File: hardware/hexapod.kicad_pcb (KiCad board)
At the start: 2 copper layers, 99.9 x 85.9 mm, 66 parts, among them J1 Conn_01x01_Pin, J10 Conn_01x01_Pin, J10_L_{3}_COXA1 Conn_01x03_Pin, J11 Conn_01x01_Pin, J11_L_{4}_COXA1 Conn_01x03_Pin, J12 Conn_01x01_Pin, J12_L_{3}_FEMUR1 Conn_01x03_Pin, J13 Conn_01x01_Pin, J13_L_{4}_FEMUR1 Conn_01x03_Pin, J14 Conn_01x01_Pin, J14_L_{3}_TIBIA1 Conn_01x03_Pin, J15 Conn_01x01_Pin, J15_L_{4}_TIBIA1 Conn_01x03_Pin, J16 Conn_01x01_Pin, J16_L_{5}_COXA1 Conn_01x03_Pin, J17 Conn_01x01_Pin, J17_L_{6}_COXA1 Conn_01x03_Pin, J18 Conn_01x01_Pin, J18_L_{5}_FEMUR1 Conn_01x03_Pin, J19 Conn_01x01_Pin, J19_L_{6}_FEMUR1 Conn_01x03_Pin, J1_L_{1}_COXA1 Conn_01x03_Pin, J2 Barrel_Jack, J20 Conn_01x01_Pin, J20_L_{5}_TIBIA1 Conn_01x03_Pin, J21 Conn_01x01_Pin, J21_L_{6}_TIBIA1 Conn_01x03_Pin, J3 Barrel_Jack, J4 Barrel_Jack, J5 Conn_01x01_Pin, J5_L_{1}_FEMUR1 Conn_01x03_Pin, J6 Conn_01x01_Pin, J6_L_{1}_TIBIA1 Conn_01x03_Pin, J7 Conn_01x01_Pin, J7_L_{2}_COXA1 Conn_01x03_Pin, J8 Conn_01x01_Pin, J8_L_{2}_FEMUR1 Conn_01x03_Pin, J9 Conn_01x01_Pin, J9_L_{2}_TIBIA1 Conn_01x03_Pin

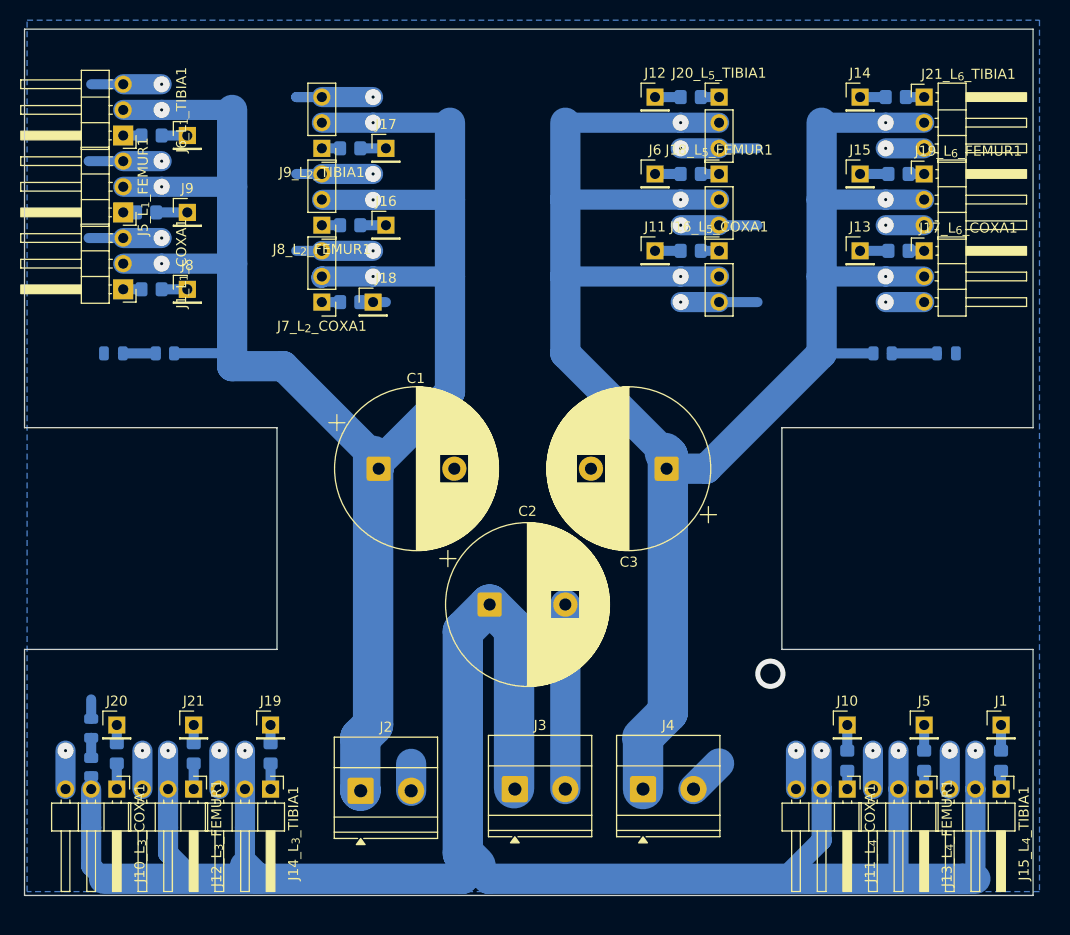
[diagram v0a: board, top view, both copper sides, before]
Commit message: add FFC connector
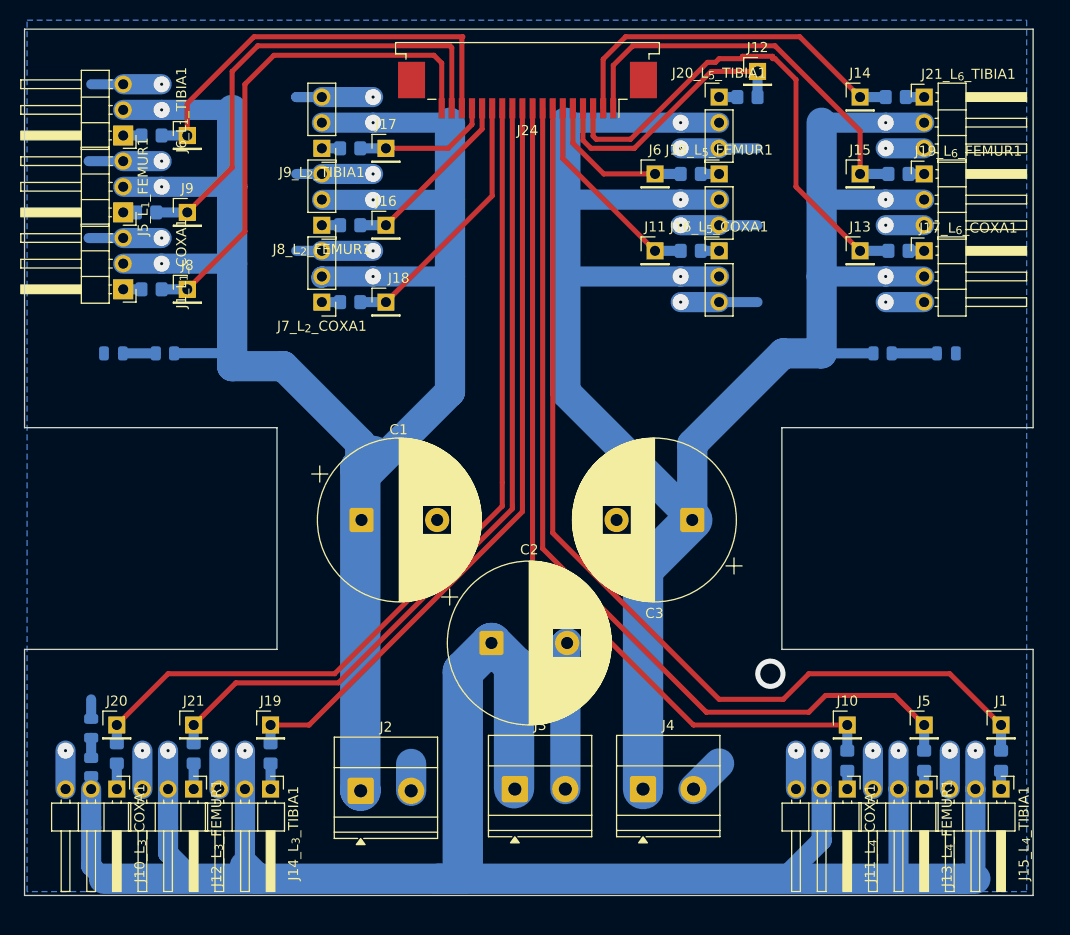
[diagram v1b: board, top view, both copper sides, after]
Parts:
- added J24: Conn_01x18, Connector_FFC-FPC:TE_1-84952-8_1x18-1MP_P1.0mm_Horizontal, F.Cu at (174.1, 51.4)
- moved J12 10.5 mm to (196.8, 49.5)
- moved C3 5.68 mm to (190.4, 94.0)
- moved R12 5.62 mm to (195.8, 52.1)
- moved C1 5.36 mm to (157.6, 94.0)
- moved C2 3.81 mm to (170.5, 106.2)
- moved J18 1.27 mm to (160.0, 72.4)
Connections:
- J1 pad 1: Net-(J1-Pin_1) -> L_{4}_TIBIA
- J10 pad 1: Net-(J10-Pin_1) -> L_{4}_COXA
- J11 pad 1: Net-(J11-Pin_1) -> L_{5}_COXA
- J12 pad 1: Net-(J12-Pin_1) -> L_{5}_TIBIA
- J13 pad 1: Net-(J13-Pin_1) -> L_{6}_COXA
- J14 pad 1: Net-(J14-Pin_1) -> L_{6}_TIBIA
- J15 pad 1: Net-(J15-Pin_1) -> L_{6}_FEMUR
- J16 pad 1: Net-(J16-Pin_1) -> L_{2}_FEMUR
- J17 pad 1: Net-(J17-Pin_1) -> L_{2}_TIBIA
- J18 pad 1: Net-(J18-Pin_1) -> L_{2}_COXA
- J19 pad 1: Net-(J19-Pin_1) -> L_{3}_TIBIA
- J20 pad 1: Net-(J20-Pin_1) -> L_{3}_COXA
- J21 pad 1: Net-(J21-Pin_1) -> L_{3}_FEMUR
- J5 pad 1: Net-(J5-Pin_1) -> L_{4}_FEMUR
- J6 pad 1: Net-(J6-Pin_1) -> L_{5}_FEMUR
- J7 pad 1: Net-(J7-Pin_1) -> L_{1}_TIBIA
- J8 pad 1: Net-(J8-Pin_1) -> L_{1}_COXA
- J9 pad 1: Net-(J9-Pin_1) -> L_{1}_FEMUR
- R10 pad 1: Net-(J10-Pin_1) -> L_{4}_COXA
- R11 pad 1: Net-(J11-Pin_1) -> L_{5}_COXA
- R12 pad 1: Net-(J12-Pin_1) -> L_{5}_TIBIA
- R13 pad 1: Net-(J13-Pin_1) -> L_{6}_COXA
- R14 pad 1: Net-(J14-Pin_1) -> L_{6}_TIBIA
- R15 pad 1: Net-(J15-Pin_1) -> L_{6}_FEMUR
- R16 pad 1: Net-(J16-Pin_1) -> L_{2}_FEMUR
- R17 pad 1: Net-(J17-Pin_1) -> L_{2}_TIBIA
- R18 pad 1: Net-(J18-Pin_1) -> L_{2}_COXA
- R19 pad 1: Net-(J19-Pin_1) -> L_{3}_TIBIA
- R20 pad 1: Net-(J20-Pin_1) -> L_{3}_COXA
- R21 pad 1: Net-(J21-Pin_1) -> L_{3}_FEMUR
- R4 pad 1: Net-(J1-Pin_1) -> L_{4}_TIBIA
- R5 pad 1: Net-(J5-Pin_1) -> L_{4}_FEMUR
- R6 pad 1: Net-(J6-Pin_1) -> L_{5}_FEMUR
- R7 pad 1: Net-(J7-Pin_1) -> L_{1}_TIBIA
- R8 pad 1: Net-(J8-Pin_1) -> L_{1}_COXA
- R9 pad 1: Net-(J9-Pin_1) -> L_{1}_FEMUR
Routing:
- net L_{4}_TIBIA: track 1.81 -> 100.9 mm
- net L_{4}_FEMUR: track 1.81 -> 94.4 mm
- net L_{3}_COXA: track 2.54 -> 91.0 mm
- net L_{4}_COXA: track 1.81 -> 87.3 mm
- net L_{3}_FEMUR: track 2.54 -> 84.5 mm
- net L_{3}_TIBIA: track 2.54 -> 78.0 mm
- net L_{1}_COXA: track 1.54 -> 52.2 mm
- net L_{6}_COXA: track 1.54 -> 51.6 mm
- net L_{1}_FEMUR: track 0.00 -> 47.3 mm
- net L_{1}_TIBIA: track 1.81 -> 44.7 mm
- net L_{6}_FEMUR: track 1.54 -> 41.6 mm
- net L_{6}_TIBIA: track 1.81 -> 38.1 mm
- net L_{5}_TIBIA: track 1.81 -> 28.3 mm
- net L_{2}_COXA: track 1.81 -> 27.9 mm
- net L_{5}_COXA: track 1.81 -> 22.3 mm
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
